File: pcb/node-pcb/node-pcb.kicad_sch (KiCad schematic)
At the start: 57 parts, among them J1 TYPE-C-31-M-12, J2 BM08B-GHS-TBT(LF)(SN), J3 BM08B-GHS-TBT(LF)(SN), J4 TC2030, J5 AFC11-S12ICA-00, Q1 S8050, SW1 TS-1187A-B-A-B, U1 NCP1117ST33T3G, U2 W25Q32JVSSIQ, U3 RP2040, U4 THVD1450DR, Y1 ABM8-272-T3

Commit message: Add BOM CSV and schematic PDF for node-pcb design
- Created a new BOM CSV file detailing components used in the node-pcb project, including specifications such as reference, description, quantity, part numbers, and links to datasheets.
- Added a new schematic PDF file for the node-pcb design to provide a visual representation of the circuit layout.
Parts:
- removed MH1, MH2, MH3, MH4: NPTH FD2.75mm SM3.15mm KO6mm, RPI_COMPILED:none_mh_npth_fd2p75mm_sm3p15mm_ko6mm, symbol RPI_DB:Mechanical | Mounting_Holes/RP-01HF5R-LCTEJS
- removed U1: NCP1117ST33T3G, Package_TO_SOT_SMD:SOT-223-3_TabPin2, symbol Regulator_Linear:NCP1117-3.3_SOT223
- added U1: AP2112K-3.3, JLCPCB:SOT-25-5_L2.9-W1.6-P0.95-LS2.8-BL, symbol Regulator_Linear:AP2112K-3.3
- C1: renamed from C6; footprint EasyEDA:C0402 -> JLCPCB:C0402; symbol EasyEDA:CL05B104KO5NNNC -> JLCPCB:CL05B104KO5NNNC
- C10: renamed from C4; footprint EasyEDA:C0805 -> JLCPCB:C0805; symbol EasyEDA:GRM21BR61C106KE15L -> JLCPCB:GRM21BR61C106KE15L
- C11: renamed from C1; footprint EasyEDA:C0805 -> JLCPCB:C0805; symbol EasyEDA:GRM21BR61C106KE15L -> JLCPCB:GRM21BR61C106KE15L
- C12: renamed from C17; footprint EasyEDA:C0805 -> JLCPCB:C0805; symbol EasyEDA:GRM21BR61C106KE15L -> JLCPCB:GRM21BR61C106KE15L
- C13: renamed from C10; footprint EasyEDA:C0402 -> JLCPCB:C0402; symbol EasyEDA:CL05A105KA5NQNC -> JLCPCB:CL05A105KA5NQNC
- C14: renamed from C8; footprint EasyEDA:C0402 -> JLCPCB:C0402; symbol EasyEDA:CL05A105KA5NQNC -> JLCPCB:CL05A105KA5NQNC
- C15: renamed from C5; footprint EasyEDA:C0402 -> JLCPCB:C0402; symbol EasyEDA:CL05B104KO5NNNC -> JLCPCB:CL05B104KO5NNNC
- C16: renamed from C20; footprint EasyEDA:C0805 -> JLCPCB:C0805; symbol EasyEDA:GRM21BR61C106KE15L -> JLCPCB:GRM21BR61C106KE15L
- C17: renamed from C2; footprint EasyEDA:C0402 -> JLCPCB:C0402; symbol EasyEDA:0402CG150J500NT -> JLCPCB:0402CG150J500NT
- C18: renamed from C3; footprint EasyEDA:C0402 -> JLCPCB:C0402; symbol EasyEDA:0402CG150J500NT -> JLCPCB:0402CG150J500NT
- C19: footprint EasyEDA:C0402 -> JLCPCB:C0402; symbol EasyEDA:CL05A105KA5NQNC -> JLCPCB:CL05A105KA5NQNC
- C2: renamed from C7; footprint EasyEDA:C0402 -> JLCPCB:C0402; symbol EasyEDA:CL05B104KO5NNNC -> JLCPCB:CL05B104KO5NNNC
- C20: renamed from C18; footprint EasyEDA:C0402 -> JLCPCB:C0402; symbol EasyEDA:CL05B104KO5NNNC -> JLCPCB:CL05B104KO5NNNC
- C3: renamed from C9; footprint EasyEDA:C0402 -> JLCPCB:C0402; symbol EasyEDA:CL05B104KO5NNNC -> JLCPCB:CL05B104KO5NNNC
- C4: renamed from C11; footprint EasyEDA:C0402 -> JLCPCB:C0402; symbol EasyEDA:CL05B104KO5NNNC -> JLCPCB:CL05B104KO5NNNC
- C5: renamed from C12; footprint EasyEDA:C0402 -> JLCPCB:C0402; symbol EasyEDA:CL05B104KO5NNNC -> JLCPCB:CL05B104KO5NNNC
- C6: renamed from C13; footprint EasyEDA:C0402 -> JLCPCB:C0402; symbol EasyEDA:CL05B104KO5NNNC -> JLCPCB:CL05B104KO5NNNC
- C7: renamed from C14; footprint EasyEDA:C0402 -> JLCPCB:C0402; symbol EasyEDA:CL05B104KO5NNNC -> JLCPCB:CL05B104KO5NNNC
- C8: renamed from C15; footprint EasyEDA:C0402 -> JLCPCB:C0402; symbol EasyEDA:CL05B104KO5NNNC -> JLCPCB:CL05B104KO5NNNC
- C9: renamed from C16; footprint EasyEDA:C0402 -> JLCPCB:C0402; symbol EasyEDA:CL05B104KO5NNNC -> JLCPCB:CL05B104KO5NNNC
- D1: renamed from D2; footprint EasyEDA:SOD-123_L2.7-W1.6-LS3.7-RD-1 -> JLCPCB:SOD-123_L2.7-W1.6-LS3.7-RD-1; symbol EasyEDA:B5819W_C8598 -> JLCPCB:B5819W_C8598
- D2: renamed from D1; footprint EasyEDA:SOD-123_L2.7-W1.6-LS3.7-RD-1 -> JLCPCB:SOD-123_L2.7-W1.6-LS3.7-RD-1; symbol EasyEDA:B5819W_C8598 -> JLCPCB:B5819W_C8598
- J1: footprint EasyEDA:USB-C_SMD-TYPE-C-31-M-12_1 -> JLCPCB:USB-C_SMD-TYPE-C-31-M-12_1; Manufacturer Korean Hroparts Elec -> (none); manufacturer_pn TYPE-C-31-M-12 -> (none)
- J2, J3: footprint EasyEDA:CONN-SMD_BM08B-GHS-TBT-LF-SN -> JLCPCB:CONN-SMD_BM08B-GHS-TBT-LF-SN; symbol EasyEDA:BM08B-GHS-TBT -> JLCPCB:BM08B-GHS-TBT
- J5: footprint EasyEDA:CONN-SMD-12P_AFC11-S12ICA-00 -> JLCPCB:CONN-SMD-12P_AFC11-S12ICA-00; symbol EasyEDA:AFC11-S12ICA-00 -> JLCPCB:AFC11-S12ICA-00
- Q1: footprint EasyEDA:SOT-23-3_L3.0-W1.7-P0.95-LS2.9-BR -> JLCPCB:SOT-23-3_L3.0-W1.7-P0.95-LS2.9-BR; symbol EasyEDA:S8050_C2146 -> JLCPCB:S8050_C2146; manufacturer_pn S8050 J3Y(RANGE:200-350) -> (none); package SOT-23 -> (none)
- R1: renamed from R7; footprint EasyEDA:R0603 -> JLCPCB:R0603; symbol EasyEDA:0603WAF5101T5E -> JLCPCB:0603WAF5101T5E
- R10: renamed from R9; footprint EasyEDA:R0402 -> JLCPCB:R0402; symbol EasyEDA:0402WGF1002TCE -> JLCPCB:0402WGF1002TCE
- R11: footprint EasyEDA:R0805 -> JLCPCB:R0805; symbol JLC_Import:0805W8F470JT5E -> JLCPCB:0805W8F470JT5E
- R12: renamed from R13; footprint EasyEDA:R0402 -> JLCPCB:R0402; symbol EasyEDA:0402WGF2201TCE -> JLCPCB:0402WGF2201TCE
- R13: renamed from R14; footprint EasyEDA:R0402 -> JLCPCB:R0402; symbol EasyEDA:0402WGF1002TCE -> JLCPCB:0402WGF1002TCE
- R2: renamed from R6; footprint EasyEDA:R0603 -> JLCPCB:R0603; symbol EasyEDA:0603WAF5101T5E -> JLCPCB:0603WAF5101T5E
- R3, R4: footprint EasyEDA:R0402 -> JLCPCB:R0402; symbol EasyEDA:0402WGF330JTCE -> JLCPCB:0402WGF330JTCE
- R5: renamed from R2; footprint EasyEDA:R0402 -> JLCPCB:R0402; symbol EasyEDA:0402WGF1002TCE -> JLCPCB:0402WGF1002TCE
- R6: renamed from R1; footprint EasyEDA:R0402 -> JLCPCB:R0402; symbol EasyEDA:0402WGF1001TCE -> JLCPCB:0402WGF1001TCE
- R7: renamed from R5; footprint EasyEDA:R0402 -> JLCPCB:R0402; symbol EasyEDA:0402WGF1001TCE -> JLCPCB:0402WGF1001TCE
- R8: renamed from R10; footprint EasyEDA:R0402 -> JLCPCB:R0402; symbol JLC_Import:0402WGF1200TCE -> JLCPCB:0402WGF1200TCE
- R9: renamed from R8; footprint EasyEDA:R0402 -> JLCPCB:R0402; symbol EasyEDA:0402WGF1002TCE -> JLCPCB:0402WGF1002TCE
- SW1: footprint EasyEDA:SW-SMD_4P-L5.1-W5.1-P3.70-LS6.5-TL_H1.5 -> JLCPCB:SW-SMD_4P-L5.1-W5.1-P3.70-LS6.5-TL_H1.5; symbol EasyEDA:TS-1187A-B-A-B -> JLCPCB:TS-1187A-B-A-B; manufacturer_pn TS-1187A-B-A-B -> (none); package SMD-4P,5.1x5.1mm -> (none)
- U2: footprint EasyEDA:SOIC-8_L5.3-W5.3-P1.27-LS8.0-BL -> JLCPCB:SOIC-8_L5.3-W5.3-P1.27-LS8.0-BL
- U3: footprint RPI_COMPILED:rpi_rp2040_vias -> JLCPCB:LQFN-56_L7.0-W7.0-P0.4-EP; symbol RPI_DB:Integrated_Circuits | Microcontrollers/RP-01EKHS-ZTKTEH -> JLCPCB:RP2040
- U4: footprint EasyEDA:SOIC-8_L4.9-W3.9-P1.27-LS6.0-BL -> JLCPCB:SOIC-8_L4.9-W3.9-P1.27-LS6.0-BL
- Y1: footprint EasyEDA:CRYSTAL-SMD_4P-L3.2-W2.5-BL -> JLCPCB:CRYSTAL-SMD_4P-L3.2-W2.5-BL; symbol RPI_DB:Frequency_Timing | Crystals/RP-01G8X7-GS352B -> JLCPCB:ABM8-272-T3_C20625731
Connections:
- net +3V3: now also U1.5 (VOUT)
- net GND: now also J1.SH (SHIELD), U1.2 (GND); no longer J1.S1 (SHIELD)
- net USB_D+: now also J1.A7 (D-), J1.B7 (D-); no longer J1.A6 (D+), J1.B6 (D+)
- net USB_D-: now also J1.A6 (D+), J1.B6 (D+); no longer J1.A7 (D-), J1.B7 (D-)
- net USB_MCU_D-: now reaches R4.1, U3.46 (USB_DM)
- net USB_MCU_D+: now reaches R3.1, U3.47 (USB_DP)
- net 5V_LOCAL: now reaches C11.1, D1.1 (-), D2.1 (-), TP1.1
- net 5V_LOCAL: now also U1.1 (VIN), U1.3 (EN)
- net VBUS_USB-C: now reaches D2.2 (+), J1.A4 (VBUS), J1.A9 (VBUS), J1.B4 (VBUS), J1.B9 (VBUS)
- net LEDA: now reaches J5.3, R11.2
- net USB-C_CC2: now reaches J1.B5 (CC2), R2.1
- net USB-C_CC1: now reaches J1.A5 (CC1), R1.1
- no-connect marks 21 -> 20
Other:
- company: (none) -> Marino Zwyssig
- moved on the sheet: C11, J1, R7

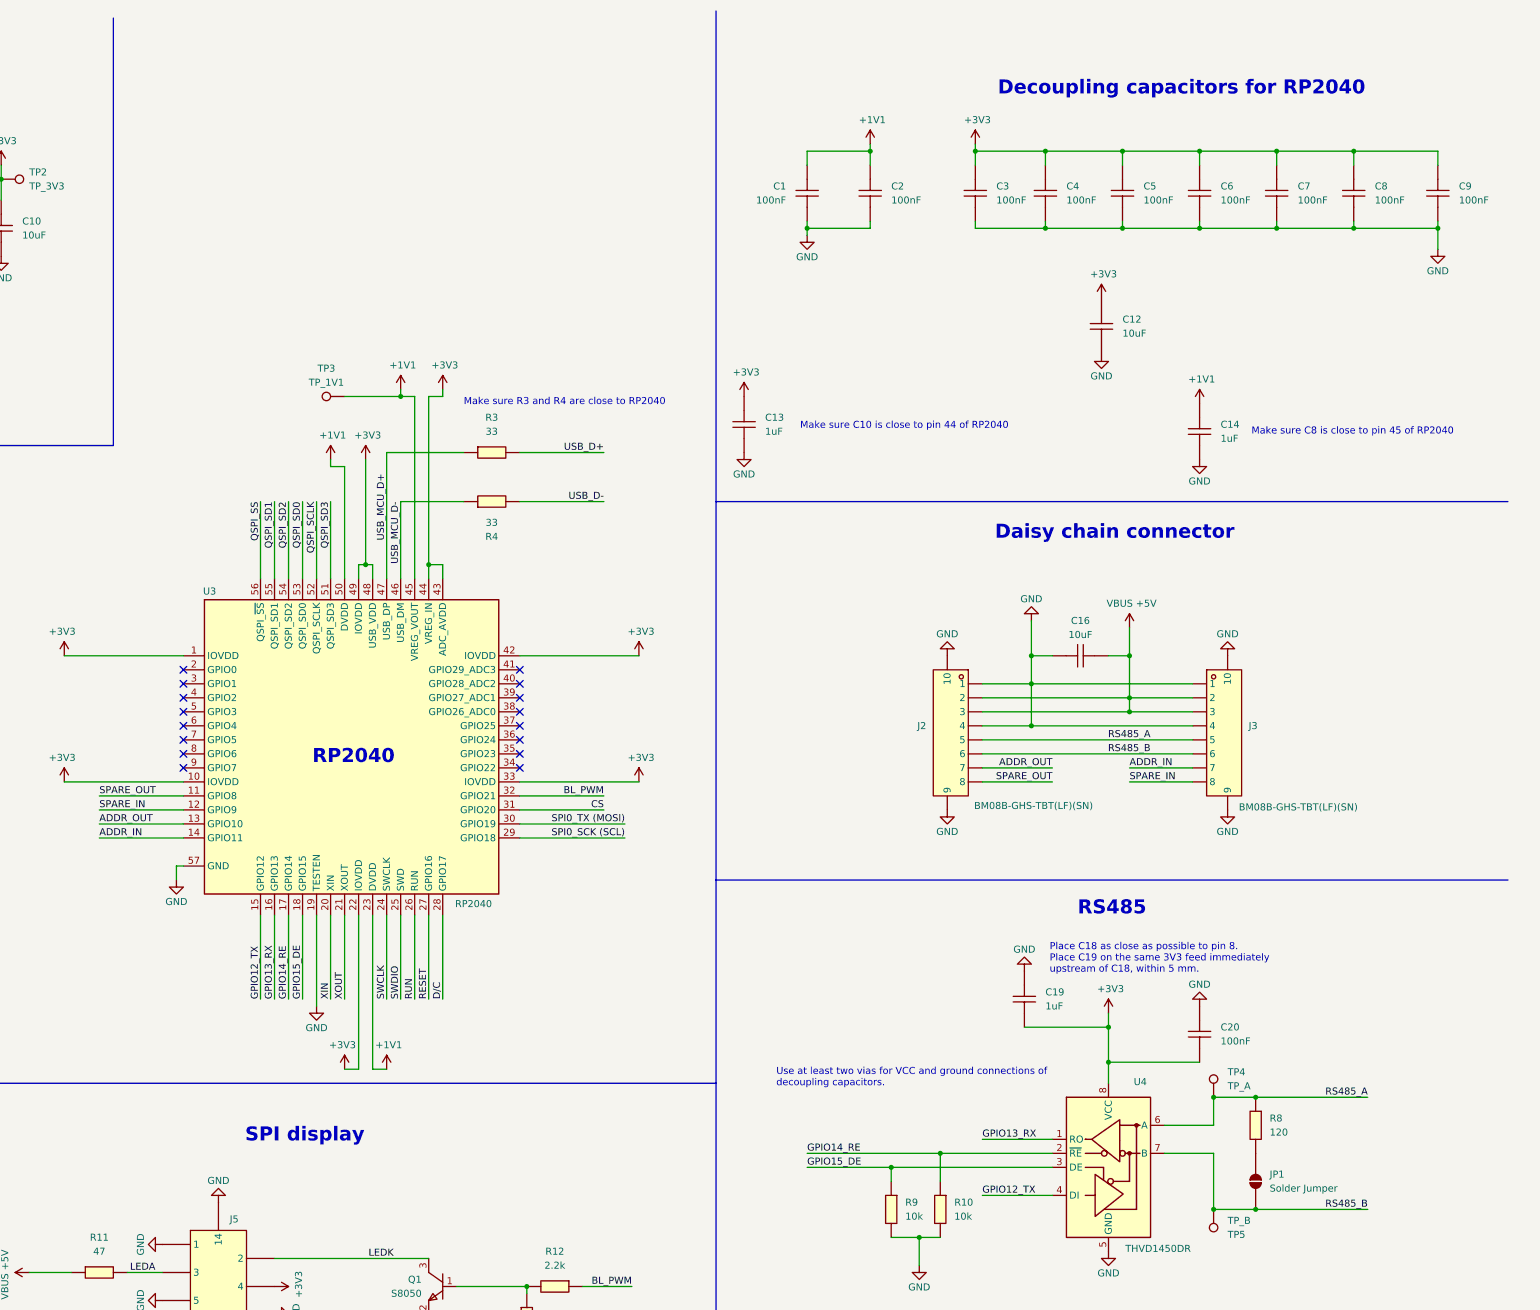
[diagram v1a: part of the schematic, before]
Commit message: Update schematic PDF with latest design revisions
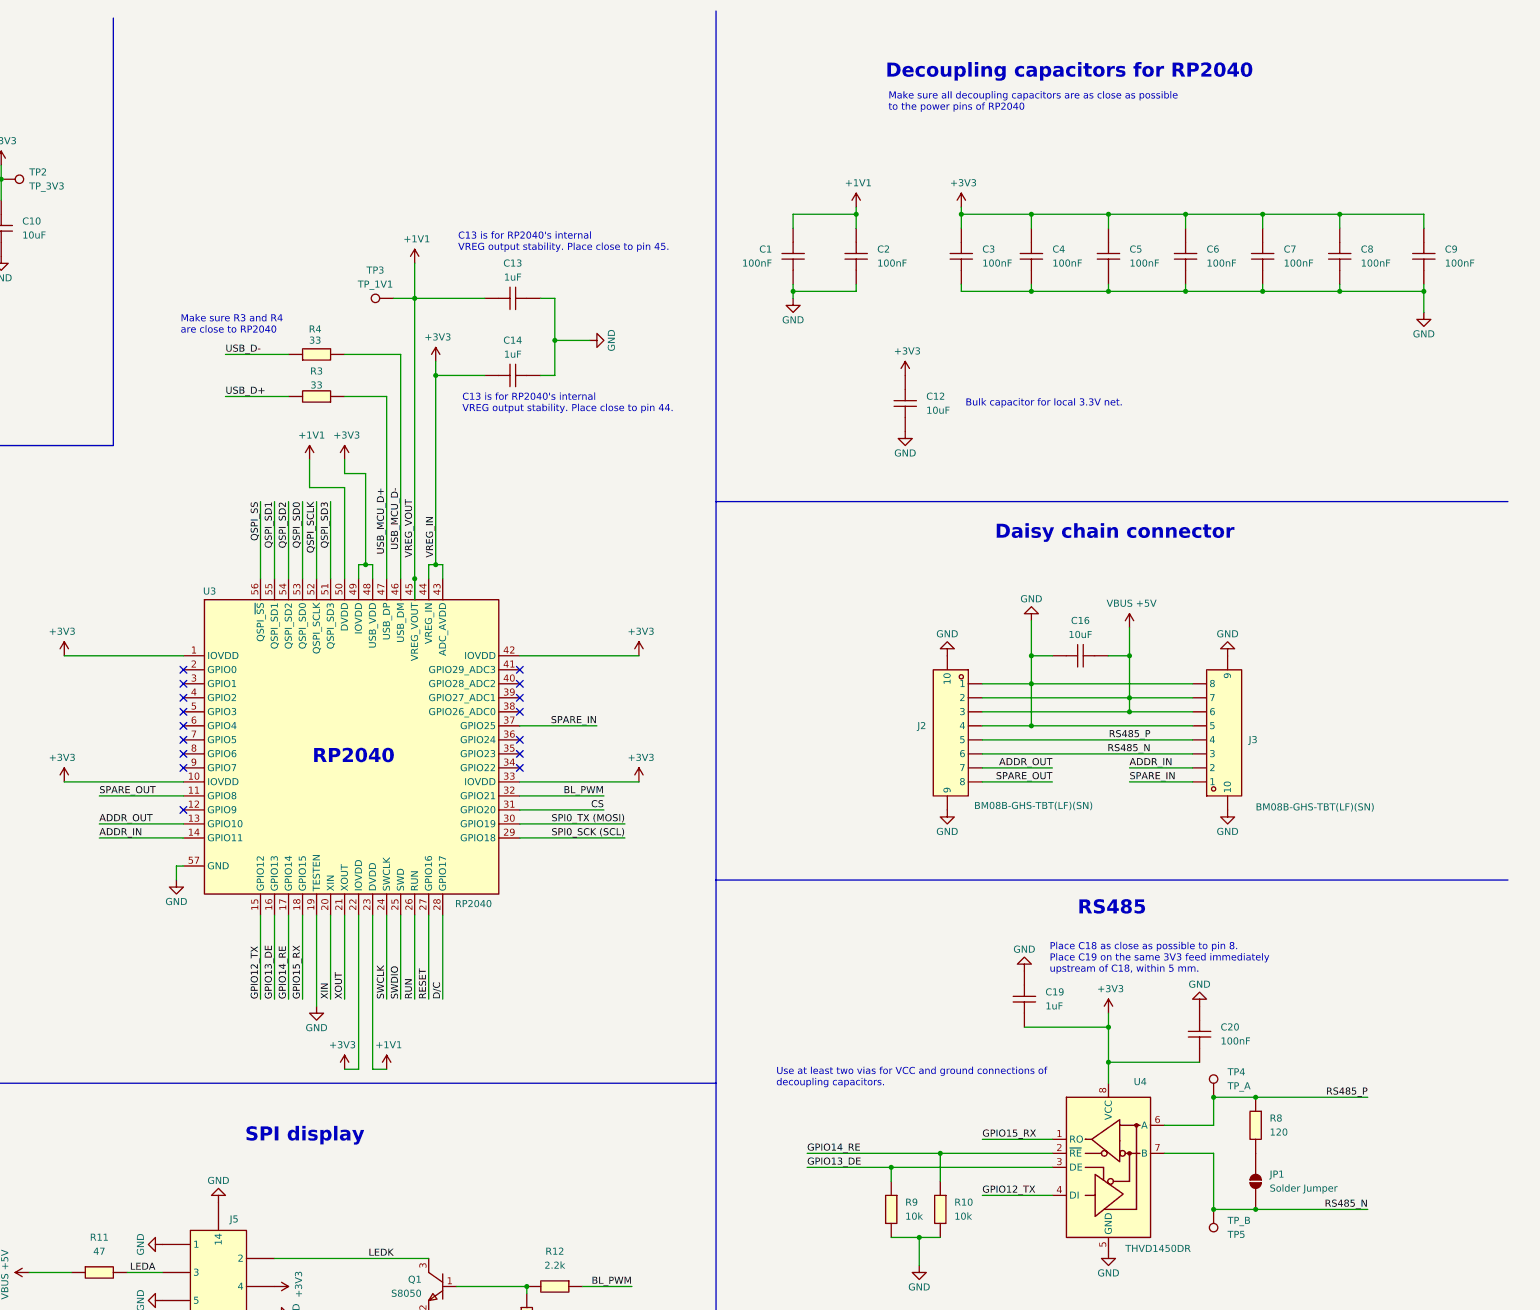
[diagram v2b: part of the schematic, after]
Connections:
- net +1V1: now also C13.2; no longer C14.1
- net +3V3: now also C14.1; no longer C13.1
- net ADDR_IN: now also J3.2; no longer J3.7
- net GND: now also C13.1, J3.5, J3.8; no longer C13.2, J3.1, J3.4
- net SPARE_IN: now also J3.1, U3.37 (GPIO25); no longer J3.8, U3.12 (GPIO9)
- net USB_D-: now also R4.1; no longer R4.2
- net USB_MCU_D-: now also R4.2; no longer R4.1
- net VBUS +5V: now also J3.6, J3.7; no longer J3.2, J3.3
- net GPIO13_RX renamed GPIO13_DE
- net GPIO13_DE: now also R9.1, U4.3 (DE); no longer U4.1 (RO)
- removed net GPIO15_DE: R9.1, U3.18 (GPIO15), U4.3 (DE)
- net RS485_A renamed RS485_P
- net RS485_P: now also J3.4; no longer J3.5
- net RS485_B renamed RS485_N
- net RS485_N: now also J3.3; no longer J3.6
- new net GPIO15_RX: U3.18 (GPIO15), U4.1 (RO)
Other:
- note added: "Bulk capacitor for local 3.3V net."
- note added: "C13 is for RP2040's internal VREG output stability. Place close to pin 44."
- note added: "C13 is for RP2040's internal VREG output stability. Place close to pin 45."
- note added: "Make sure all decoupling capacitors are as close as possible to the power pins of RP2040"
- note removed: "Make sure C10 is close to pin 44 of RP2040"
- note removed: "Make sure C8 is close to pin 45 of RP2040"
- moved on the sheet: C1, C12, C2, C3, C4, C5, C6, C7, C8, C9, R3, R4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

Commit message: Refactor PCB and schematic files for improved clarity and functionality
- Updated PCB netclass assignments from "Power" to "Default" for better consistency.
- Changed PCB color settings to transparent for the "Power" netclass.
- Adjusted clearance value for the "QSPI" netclass from 0.3 to 0.2.
- Removed redundant no_connect entries and added a new no_connect entry in the schematic.
- Added new wire connections in the schematic for better signal integrity.
- Renamed label "ADDR_IN" to "SPARE_IN" and adjusted its position, while creating a new "ADDR_IN" label at a different location.
- Cleaned up used designators in the PCB file for better organization.
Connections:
- net ADDR_IN: now also U3.12 (GPIO9); no longer U3.14 (GPIO11)
- net SPARE_IN: now also U3.14 (GPIO11); no longer U3.37 (GPIO25)
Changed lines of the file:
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@@
+	)
+	(no_connect
+		(at 228.6 140.97)
 	)
 	(no_connect
@@
 	)
 	(no_connect
-		(at 167.64 156.21)
-	)
-	(no_connect
 		(at 167.64 140.97)
 	)
@@
 	(wire
 		(pts
+			(xy 43.18 41.91) (xy 63.5 41.91)
+		)
+		(stroke
+			(width 0)
+			(type default)
+		)
+	)
+	(wire
+		(pts
 			(xy 289.56 46.99) (xy 289.56 48.26)
 		)
@@
 	(wire
 		(pts
-			(xy 228.6 140.97) (xy 242.57 140.97)
-		)
-		(stroke
-			(width 0)
-			(type default)
-		)
-	)
-	(wire
-		(pts
 			(xy 196.85 73.66) (xy 207.01 73.66)
 		)
@@
 	(wire
 		(pts
-			(xy 43.18 41.91) (xy 63.5 41.91)
-		)
-		(stroke
-			(width 0)
-			(type default)
-		)
-	)
-	(wire
-		(pts
 			(xy 349.25 50.8) (xy 349.25 48.26)
 		)
@@
 		(pts
 			(xy 308.61 48.26) (xy 308.61 50.8)
+		)
+		(stroke
+			(width 0)
+			(type default)
+		)
+	)
+	(wire
+		(pts
+			(xy 152.4 156.21) (xy 167.64 156.21)
 		)
 		(stroke
@@
 		)
 	)
-	(label "SPARE_IN"
-		(at 242.57 140.97 180)
-		(effects
-			(font
-				(size 1.27 1.27)
-			)
-			(justify right bottom)
-		)
-	)
 	(label "USB_D+"
 		(at 76.2 54.61 180)
@@
 		)
 	)
-	(label "ADDR_IN"
+	(label "SPARE_IN"
 		(at 152.4 161.29 0)
 		(effects
@@
 		(effects
 			(font
+				(size 1.27 1.27)
+			)
+			(justify left bottom)
+		)
+	)
+	(label "ADDR_IN"
+		(at 152.4 156.21 0)
+		(effects
+			(font

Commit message: Update schematic PDF with latest design revisions
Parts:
- removed TP4: TP_A, TestPoint:TestPoint_Pad_D1.0mm, symbol Connector:TestPoint
- removed TP5: TP_B, TestPoint:TestPoint_Pad_D1.0mm, symbol Connector:TestPoint
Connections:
- net 5V_LOCAL: now also R11.1
- net VBUS +5V renamed +5V_BUS
- net +5V_BUS: no longer R11.1
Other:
- note added: "C14 is for RP2040's internal VREG input stability. Place close to pin 44."
- note removed: "C13 is for RP2040's internal VREG output stability. Place close to pin 44."

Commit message: Refactor BOM CSV for component grouping and update part references
- Consolidated multiple entries for ceramic capacitors into grouped lines for better readability and management.
- Updated the header of the BOM CSV to reflect changes in part categorization.
- Added new entries for components with extended and basic classifications.
- Introduced a lock file for KiCad project to track user session.
- Updated schematic PDF to reflect recent changes in the design.
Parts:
- added R14, R15, R16, R17: 1k, JLCPCB:R0402, symbol JLCPCB:0402WGF1001TCE
- C1, C13, C14, C15, C17, C18, C19, C2, C20, C3, C4, C5, C6, C7, C8, C9, D1, D2, Q1, R1, R10, R11, R12, R13, R2, R3, R4, R6, R7, R8, R9, SW1: JLCPCB Parts Type (none) -> Basic
- C10: JLCPCB Parts Type (none) -> Basic; LCSC Part C77075 -> C15850; MPN GRM21BR61C106KE15L -> CL21A106KAYNNNE; Manufacturer Murata Electronics -> Samsung Electro-Mechanics; manufacturer_pn GRM21BR61C106KE15L -> CL21A106KAYNNNE; voltage 16V -> 25 V
- C11, C12, C16: JLCPCB Parts Type (none) -> Basic; LCSC Part C77075 -> C15850; Manufacturer Murata Electronics -> Samsung Electro-Mechanics; voltage 16V -> 25 V
- J1, J2, J3, J5, U1, U2, U3, U4, Y1: JLCPCB Parts Type (none) -> Extended
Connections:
- net ADDR_IN: now also R16.1; no longer J3.2
- net ADDR_OUT: now also R14.2; no longer J2.7
- net GND: now also J1.A1B12 (GND), J1.B1A12 (GND); no longer J1.A1 (GND), J1.A12 (GND), J1.B1 (GND), J1.B12 (GND)
- net SPARE_IN: now also R17.1; no longer J3.1
- net SPARE_OUT: now also R15.2; no longer J2.8
- net USB_D+: now also J1.A6 (D+), J1.B6 (D+); no longer J1.A7 (D-), J1.B7 (D-)
- net USB_D-: now also J1.A7 (D-), J1.B7 (D-); no longer J1.A6 (D+), J1.B6 (D+)
- net VBUS_USB-C: now also J1.A4B9 (VBUS), J1.B4A9 (VBUS); no longer J1.A4 (VBUS), J1.A9 (VBUS), J1.B4 (VBUS), J1.B9 (VBUS)
- net GPIO13_DE renamed GPIO14_DE
- net GPIO14_DE: now also U3.17 (GPIO14); no longer U3.16 (GPIO13)
- net GPIO14_RE renamed GPIO15_RE
- net GPIO15_RE: now also U3.18 (GPIO15); no longer U3.17 (GPIO14)
- net GPIO15_RX renamed GPIO13_RX
- net GPIO13_RX: now also U3.16 (GPIO13); no longer U3.18 (GPIO15)
- new net: J2.7, R14.1
- new net: J2.8, R15.1
- new net: J3.1, R17.2
- new net: J3.2, R16.2
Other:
- note added: "Note: The pin numbering of the connectors are flipped, because the footprints are mirrored in the layout. This is intentional."
- note added: "Place C20 as close as possible to pin 8. Place C19 on the same 3V3 feed immediately upstream of C20, within 5 mm."
- note removed: "Place C18 as close as possible to pin 8. Place C19 on the same 3V3 feed immediately upstream of C18, within 5 mm."
- moved on the sheet: J2, J3
